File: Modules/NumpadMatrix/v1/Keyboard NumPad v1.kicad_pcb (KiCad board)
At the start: 2 copper layers, 80.2 x 123 mm, 45 parts, among them U2 ESP32-C3_SUPERMINI_SMD

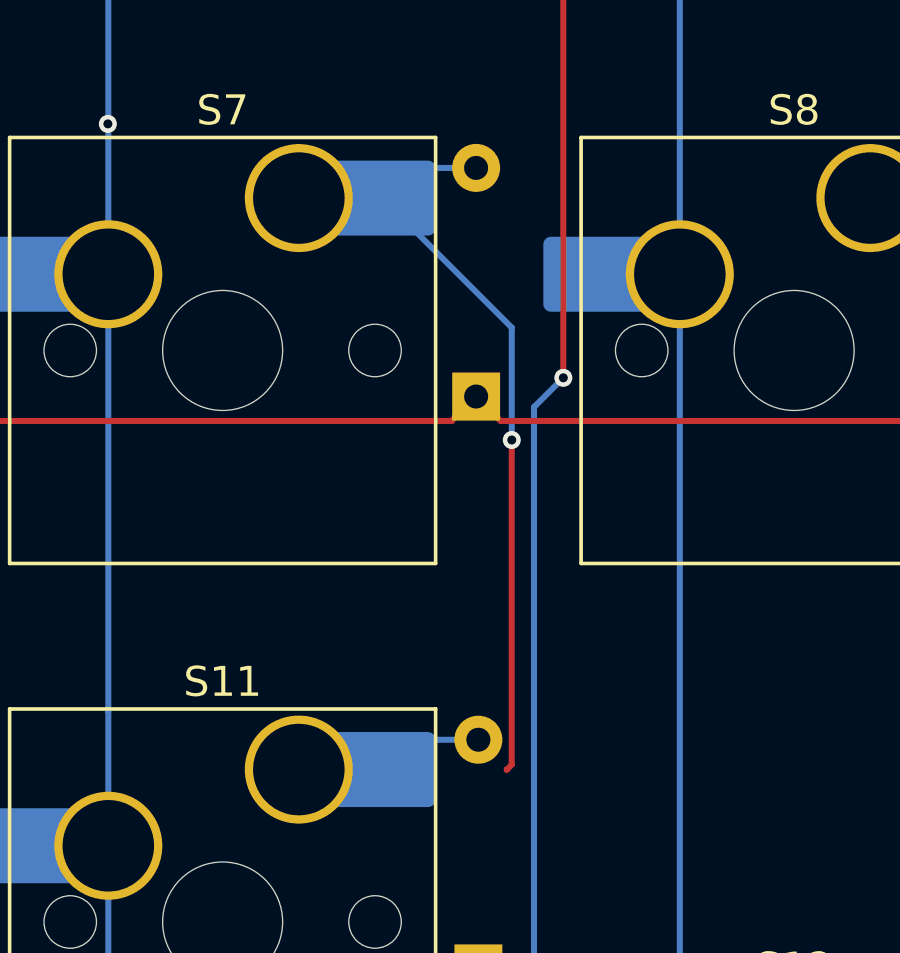
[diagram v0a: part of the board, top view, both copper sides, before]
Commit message: iniciated the ControlerBoard V0. I need the screen size!!
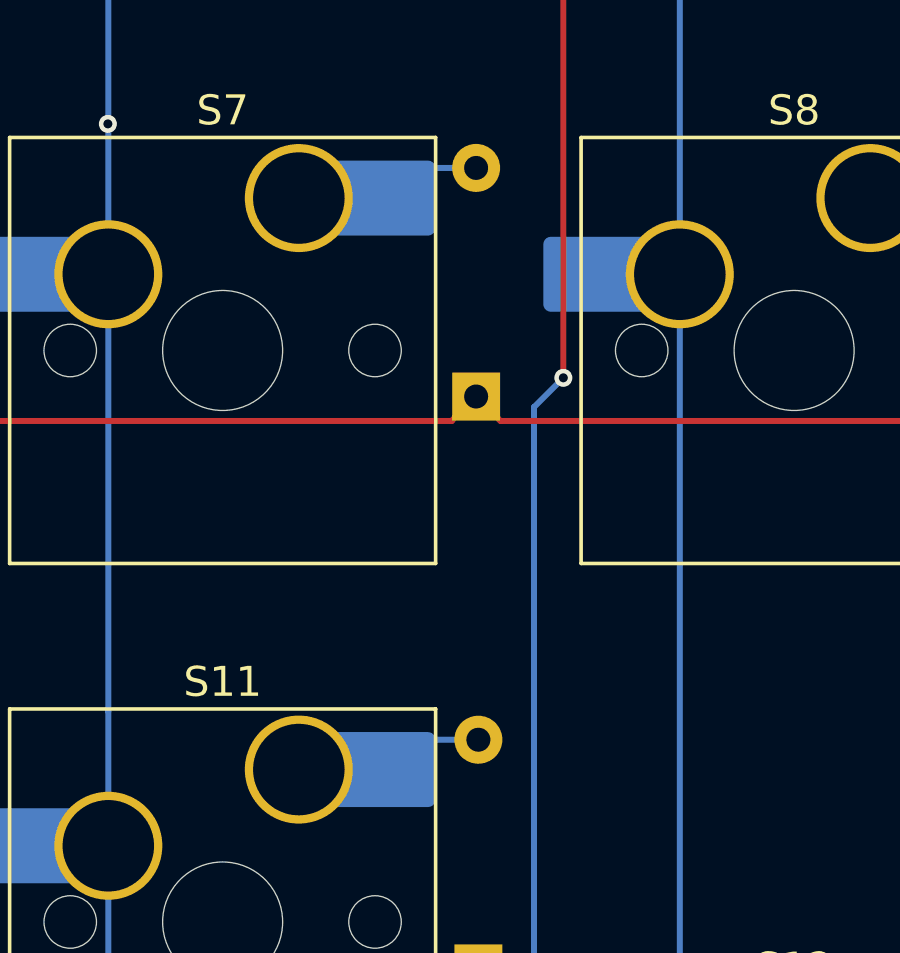
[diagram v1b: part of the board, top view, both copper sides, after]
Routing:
- net Net-(D7-A): track 28.0 -> 6.33 mm, vias 1 -> 0
